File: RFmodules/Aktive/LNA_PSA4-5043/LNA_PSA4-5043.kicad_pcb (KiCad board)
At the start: 2 copper layers, 18 x 7.6 mm, 7 parts, among them J1 SMA, J2 SMA, U1 PSA4-5043+

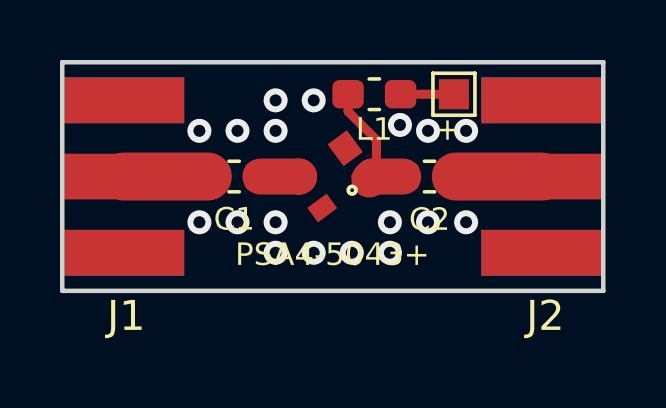
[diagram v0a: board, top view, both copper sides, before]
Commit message: Fix design guide issues
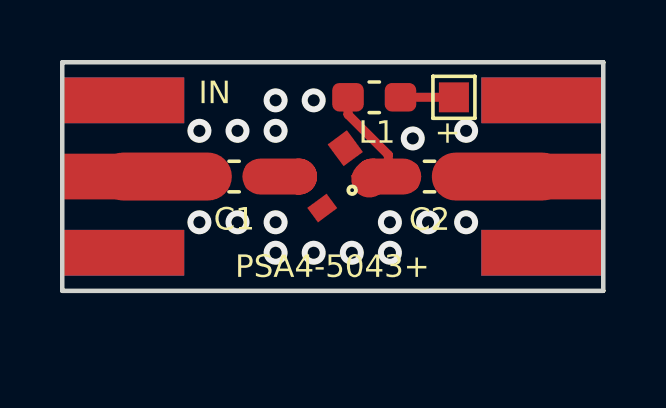
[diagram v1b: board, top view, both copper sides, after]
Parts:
- removed J1: SMA, RFLego_Footprint:SMA_Edge
- added IN: SMA, RFLego_Footprint:SMA_Edge, F.Cu at (128.0, 89.7)
- moved L1 0.10 mm to (138.4, 87.0)
- moved + 0.10 mm to (141.1, 87.0)
- renumbered J2 to OUT
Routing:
- net Net-(C2-Pad2): track 4.44 -> 5.08 mm
- net GND: vias 18 -> 17
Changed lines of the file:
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@@
   (page A4)
   (layers
-    (0 F.Cu signal hide)
+    (0 F.Cu signal)
     (31 B.Cu signal)
     (32 B.Adhes user)
@@
   (module RFLego_Footprint:SMA_Edge (layer F.Cu)
     (at 128.016 89.662)
-    (fp_text reference J1 (at 2.1336 4.6482) (layer F.SilkS)
-      (effects (font (size 1 1) (thickness 0.15)))
+    (fp_text reference IN (at 5.08 -2.794) (layer F.SilkS)
+      (effects (font (size 0.75 0.75) (thickness 0.15)))
     )
     (fp_text value SMA (at 1.27 6.35) (layer F.Fab) hide
@@
   (module RFLego_Footprint:SMA_Edge (layer F.Cu)
     (at 141.986 89.662)
-    (fp_text reference J2 (at 2.1336 4.6482) (layer F.SilkS)
-      (effects (font (size 1 1) (thickness 0.15)))
+    (fp_text reference OUT (at 0.00762 2.81178) (layer F.SilkS) hide
+      (effects (font (size 0.75 0.75) (thickness 0.15)))
     )
     (fp_text value SMA (at 1.27 6.35) (layer F.Fab) hide
@@
       (effects (font (size 1 0.9) (thickness 0.05)))
     )
-    (fp_text value PSA4-5043+ (at -2.096882 -1.548067) (layer F.SilkS)
-      (effects (font (size 0.75 0.75) (thickness 0.15)))
-    )
-    (fp_line (start -1 -0.55) (end 1 -0.55) (layer Dwgs.User) (width 0.2032))
-    (fp_line (start 1 0.55) (end -1 0.55) (layer Dwgs.User) (width 0.2032))
+    (fp_text value PSA4-5043+ (at -2.417858 -1.784711) (layer F.SilkS)
+      (effects (font (size 0.75 0.75) (thickness 0.15)))
+    )
+    (fp_line (start -1 -0.55) (end 0.999999 -0.55) (layer Dwgs.User) (width 0.2032))
+    (fp_line (start 1 0.55) (end -0.999999 0.55) (layer Dwgs.User) (width 0.2032))
     (fp_poly (pts (xy 0.150171 0.6) (xy 0.85 0.6) (xy 0.85 1.10126) (xy 0.150171 1.10126)) (layer Dwgs.User) (width 0))
     (fp_poly (pts (xy -0.851089 0.6) (xy -0.45 0.6) (xy -0.45 1.10141) (xy -0.851089 1.10141)) (layer Dwgs.User) (width 0))
@@
   )
   (module Inductor_SMD:L_0603_1608Metric_Pad1.05x0.95mm_HandSolder (layer F.Cu)
-    (at 138.4186 86.9188 180)
+    (at 138.416 87.0204 180)
     (descr "Capacitor SMD 0603 (1608 Metric), square (rectangular) end terminal, IPC_7351 nominal with elongated pad for handsoldering. (Body size source: http://www.tortai-tech.com/upload/download/2011102023233369053.pdf), generated with kicad-footprint-generator")
     (tags "inductor handsolder")
     (attr smd)
-    (fp_text reference L1 (at 0.00384 -1.1684 180) (layer F.SilkS)
+    (fp_text reference L1 (at -0.0902 -1.1684 180) (layer F.SilkS)
       (effects (font (size 0.75 0.75) (thickness 0.15)))
     )
@@
   )
   (module TestPoint:TestPoint_Pad_1.0x1.0mm (layer F.Cu)
-    (at 141.0716 86.9188)
+    (at 141.0716 87.0204)
     (descr "SMD rectangular pad as test Point, square 1.0mm side length")
     (tags "test point SMD pad rectangle square")
@@
   (via (at 135.128 87.122) (size 0.8) (drill 0.4) (layers F.Cu B.Cu) (net 1))
   (via (at 136.398 87.122) (size 0.8) (drill 0.4) (layers F.Cu B.Cu) (net 1))
-  (via (at 140.208 88.138) (size 0.8) (drill 0.4) (layers F.Cu B.Cu) (net 1))
   (via (at 141.478 88.138) (size 0.8) (drill 0.4) (layers F.Cu B.Cu) (net 1))
-  (via (at 139.27328 87.94242) (size 0.8) (drill 0.4) (layers F.Cu B.Cu) (net 1))
+  (via (at 139.7 88.392) (size 0.8) (drill 0.4) (layers F.Cu B.Cu) (net 1))
   (segment (start 132.87 89.662) (end 130.048 89.662) (width 1.6) (layer F.Cu) (net 2))
   (segment (start 135.908977 89.662) (end 135.911873 89.664896) (width 1.2) (layer F.Cu) (net 3))
@@
   (segment (start 138.350389 89.662) (end 138.250706 89.761683) (width 1.2) (layer F.Cu) (net 5))
   (segment (start 139.3838 89.662) (end 138.350389 89.662) (width 1.2) (layer F.Cu) (net 5))
-  (segment (start 137.5436 87.4938) (end 138.488896 88.439096) (width 0.3) (layer F.Cu) (net 5))
   (segment (start 138.488896 89.286335) (end 138.132127 89.643104) (width 0.3) (layer F.Cu) (net 5))
-  (segment (start 138.488896 88.439096) (end 138.488896 89.286335) (width 0.3) (layer F.Cu) (net 5))
-  (segment (start 137.5436 86.9188) (end 137.5436 87.4938) (width 0.3) (layer F.Cu) (net 5))
-  (segment (start 139.2936 86.9188) (end 141.0716 86.9188) (width 0.3) (layer F.Cu) (net 6))
+  (segment (start 138.884728 89.162928) (end 139.3838 89.662) (width 0.3) (layer F.Cu) (net 5))
+  (segment (start 137.541 87.5954) (end 138.884728 88.939128) (width 0.3) (layer F.Cu) (net 5))
+  (segment (start 138.884728 88.939128) (end 138.884728 89.162928) (width 0.3) (layer F.Cu) (net 5))
+  (segment (start 137.541 87.0204) (end 137.541 87.5954) (width 0.3) (layer F.Cu) (net 5))
+  (segment (start 139.291 87.0204) (end 141.0716 87.0204) (width 0.3) (layer F.Cu) (net 6))
   (zone (net 1) (net_name GND) (layer F.Cu) (hatch edge 0.508)
     (connect_pads yes (clearance 0.1))

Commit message: Fix typos
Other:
- board text added: "LNA PSA4-5043+ Revision 0.1.0 - 01/2019 github.com/fgaletsee/RFLego"
- board text removed: "PSA4-5043+ Revision 0.1.0 - 01/2019 github.com/fgaletsee/RFLego"
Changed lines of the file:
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@@
       (net 6 "Net-(L1-Pad1)"))
   )
-  (gr_text "PSA4-5043+\nRevision 0.1.0 - 01/2019\ngithub.com/fgaletsee/RFLego" (at 136.906 89.0016) (layer B.SilkS)
+  (gr_text "LNA PSA4-5043+\nRevision 0.1.0 - 01/2019\ngithub.com/fgaletsee/RFLego" (at 136.906 89.0016) (layer B.SilkS)
     (effects (font (size 0.75 0.75) (thickness 0.1875)))
   )

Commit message: Update board descriptions, add Bandstop elliptic filter 5th order
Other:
- board text added: "LNA PSA4-5043+ Revision 1 - 01/2019 github.com/fgaletsee/RFLego"
- board text removed: "LNA PSA4-5043+ Revision 0.1.0 - 01/2019 github.com/fgaletsee/RFLego"
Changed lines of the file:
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@@
       (net 6 "Net-(L1-Pad1)"))
   )
-  (gr_text "LNA PSA4-5043+\nRevision 0.1.0 - 01/2019\ngithub.com/fgaletsee/RFLego" (at 136.906 89.0016) (layer B.SilkS)
+  (gr_text "LNA PSA4-5043+\nRevision 1 - 01/2019\ngithub.com/fgaletsee/RFLego" (at 136.906 89.0016) (layer B.SilkS)
     (effects (font (size 0.75 0.75) (thickness 0.1875)))
   )

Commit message: Update LNA PSA4-5043 module to use new template
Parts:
- removed +: TestPoint, TestPoint:TestPoint_Pad_1.0x1.0mm
- removed IN, OUT: SMA, RFLego_Footprint:SMA_Edge
- added C3: C, Capacitor_SMD:C_0603_1608Metric_Pad1.05x0.95mm_HandSolder, F.Cu at (120.9, 104.0)
- added C4: C, Capacitor_SMD:C_0603_1608Metric_Pad1.05x0.95mm_HandSolder, F.Cu at (124.4, 109.0)
- added GND: GND, TestPoint:TestPoint_Pad_1.0x1.0mm, F.Cu at (113.0, 101.0)
- added H1: MountingHole_Pad, MountingHole:MountingHole_2.2mm_M2_Pad_Via, F.Cu at (102.2, 102.2)
- added H2: MountingHole_Pad, MountingHole:MountingHole_2.2mm_M2_Pad_Via, F.Cu at (102.2, 115.8)
- added H3: MountingHole_Pad, MountingHole:MountingHole_2.2mm_M2_Pad_Via, F.Cu at (129.8, 102.2)
- added H4: MountingHole_Pad, MountingHole:MountingHole_2.2mm_M2_Pad_Via, F.Cu at (129.8, 115.8)
- added J1: SMA, RFLego_Footprint:SMA_Edge, F.Cu at (100.0, 109.0)
- added J2: SMA, RFLego_Footprint:SMA_Edge, F.Cu at (128.0, 109.0)
- added REF**: OSHW-Logo2_9.8x8mm_SilkScreen, Symbol:OSHW-Logo2_9.8x8mm_SilkScreen, B.Cu at (109.5, 113.0)
- added VCC: VCC, TestPoint:TestPoint_Pad_1.0x1.0mm, F.Cu at (120.0, 101.0)
- C1, C2: value 10 nF -> C
- moved C1 32.2 mm to (108.0, 109.0)
- moved U1 29.1 mm to (115.3, 109.0)
- moved L1 28.0 mm to (120.0, 108.1), turned to 270 degrees
- moved C2 25.0 mm to (120.9, 105.5)
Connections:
- C2 pad 1: Net-(C2-Pad1) -> GND
- L1 pad 1: Net-(L1-Pad1) -> Net-(C2-Pad2)
- L1 pad 2: Net-(C2-Pad2) -> Net-(C4-Pad2)
- U1 pad 1: Net-(C2-Pad2) -> Net-(C4-Pad2)
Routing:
- net Net-(C4-Pad2): track 0.00 -> 6.37 mm
- net Net-(C4-Pad1): track 0.00 -> 4.75 mm
- net Net-(C1-Pad1): track 1.29 -> 5.13 mm
- net Net-(C2-Pad1): track 2.88 -> 0.00 mm
- net Net-(C1-Pad2): track 2.82 -> 5.02 mm
- net Net-(L1-Pad1): track 1.78 -> 0.00 mm
- net Net-(C2-Pad2): track 5.08 -> 6.25 mm
- net GND: vias 17 -> 121
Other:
- board size 18 x 7.6 mm -> 32 x 18 mm
- net class 0603 removed
- net class 50 Ohm thin added: clearance 0.19, trace_width 1, via_dia 0.7, via_drill 0.4
- net class 50Ohm added: clearance 0.32, trace_width 1.5, via_dia 0.7, via_drill 0.4
- net class Default: trace_width 0.3 -> 0.22; via_dia 0.8 -> 0.7
- net class RF removed
- rule via_min_size: 0.4 -> 0.6
- board text added: "PSA4-5043+ Revision 2 - 02/2019 github.com/fgaletsee/RFLego"
- board text removed: "LNA PSA4-5043+ Revision 1 - 01/2019 github.com/fgaletsee/RFLego"
